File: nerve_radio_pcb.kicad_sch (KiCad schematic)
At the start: 12 parts, among them J1 2x15, J2 5V UART Breakout, J3 3V SPI Breakout, J4 5V GPIO Breakout, U1 XBP9B-DMWT-002, U2 TXB0104QPWRQ1

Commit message: Fix board-to-board connector pinout
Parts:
- removed J1: 2x15, Connector_PinHeader_1.27mm:PinHeader_2x15_P1.27mm_Vertical_SMD, symbol Connector_Generic:Conn_02x15_Counter_Clockwise
- added J1: 2x15, Connector_PinHeader_1.27mm:PinHeader_2x15_P1.27mm_Vertical_SMD, symbol Connector_Generic:Conn_02x15_Odd_Even
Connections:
- net +3V3: now also J1.3 (Pin_3), J1.4 (Pin_4)
- net +5V: now also J1.1 (Pin_1), J1.2 (Pin_2)
- net GND: now also J1.10 (Pin_10), J1.13 (Pin_13), J1.14 (Pin_14), J1.19 (Pin_19), J1.20 (Pin_20), J1.22 (Pin_22), J1.23 (Pin_23), J1.26 (Pin_26), J1.27 (Pin_27), J1.5 (Pin_5), J1.7 (Pin_7)
- net GPIO_1: now also J1.16 (Pin_16)
- net GPIO_2: now also J1.18 (Pin_18)
- net RADIO_NRST: now also J1.12 (Pin_12)
- net RADIO_UART_CTS: now also J1.11 (Pin_11)
- net RADIO_UART_RTS: now also J1.9 (Pin_9)
- net RADIO_UART_RX: now also J1.8 (Pin_8)
- net RADIO_UART_TX: now also J1.6 (Pin_6)
- net SPI_CLK: now also J1.17 (Pin_17)
- net SPI_CS: now also J1.15 (Pin_15)
- net SPI_MISO: now also J1.21 (Pin_21)
- net SPI_MOSI: now also J1.25 (Pin_25)
- net UART_RX: now also J1.24 (Pin_24)
- net UART_TX: now also J1.28 (Pin_28)
- new net: J1.29 (Pin_29), J1.30 (Pin_30)

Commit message: Cleanup revision and docs pictures
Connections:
- net RADIO_UART_CTS: now also J1.8 (Pin_8); no longer J1.11 (Pin_11)
- net RADIO_UART_RTS: now also J1.6 (Pin_6); no longer J1.9 (Pin_9)
- net RADIO_UART_RX: now also J1.9 (Pin_9); no longer J1.8 (Pin_8)
- net RADIO_UART_TX: now also J1.11 (Pin_11); no longer J1.6 (Pin_6)

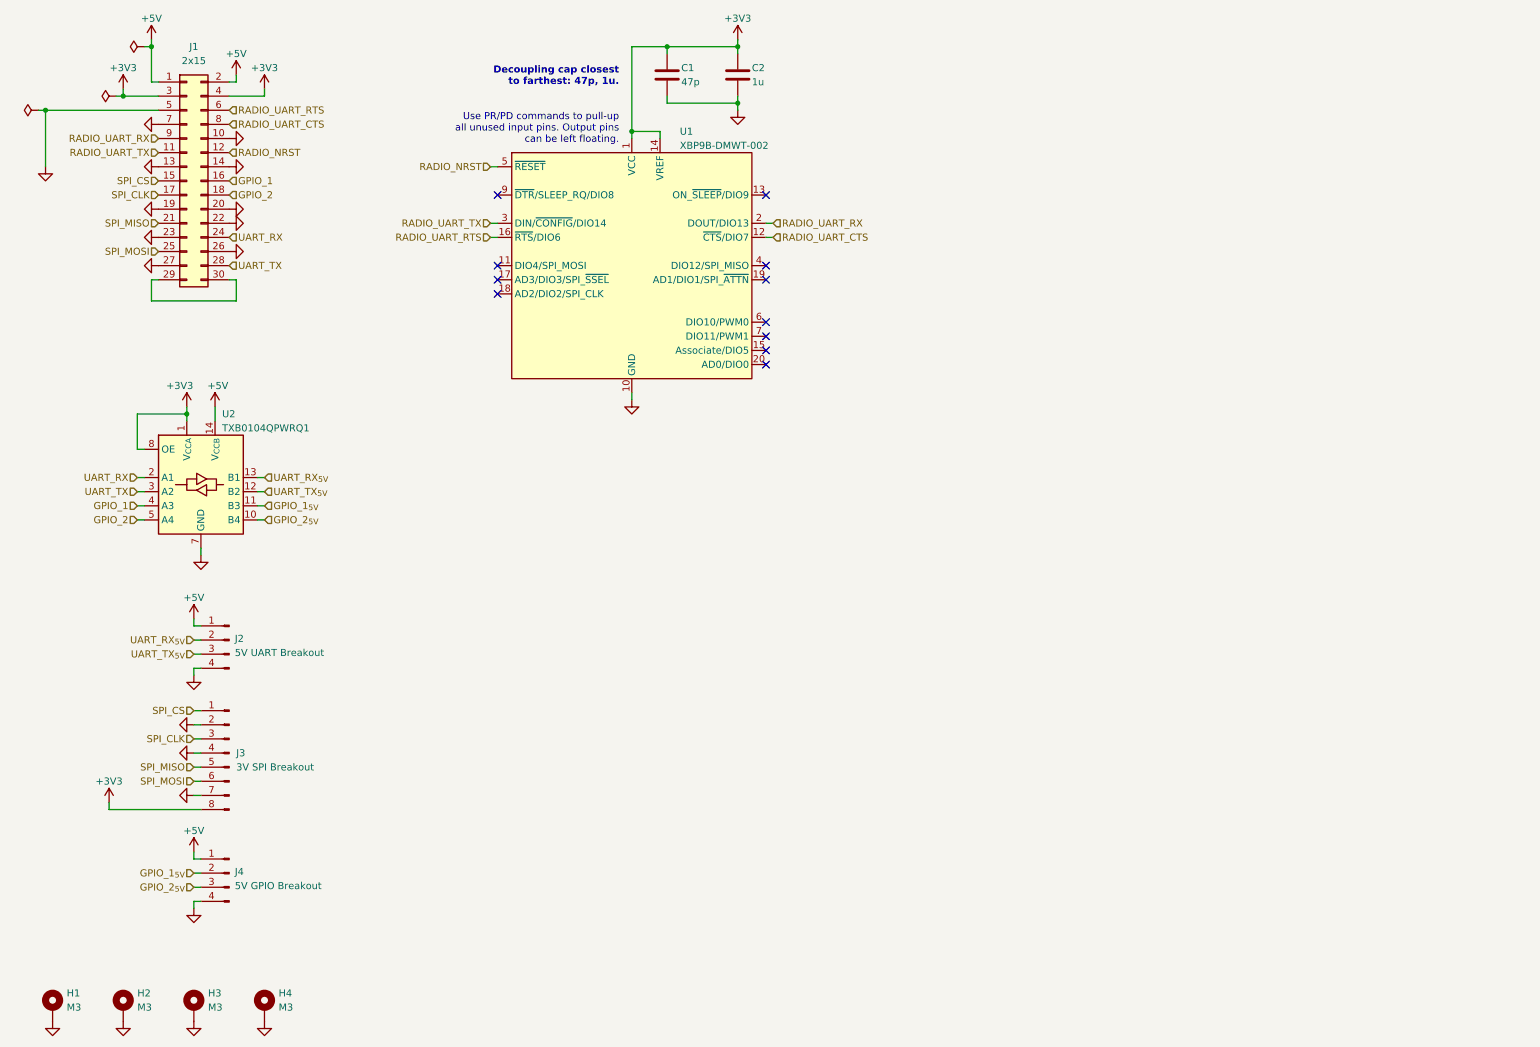
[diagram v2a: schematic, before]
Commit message: Cleanup and update board-to-board connector
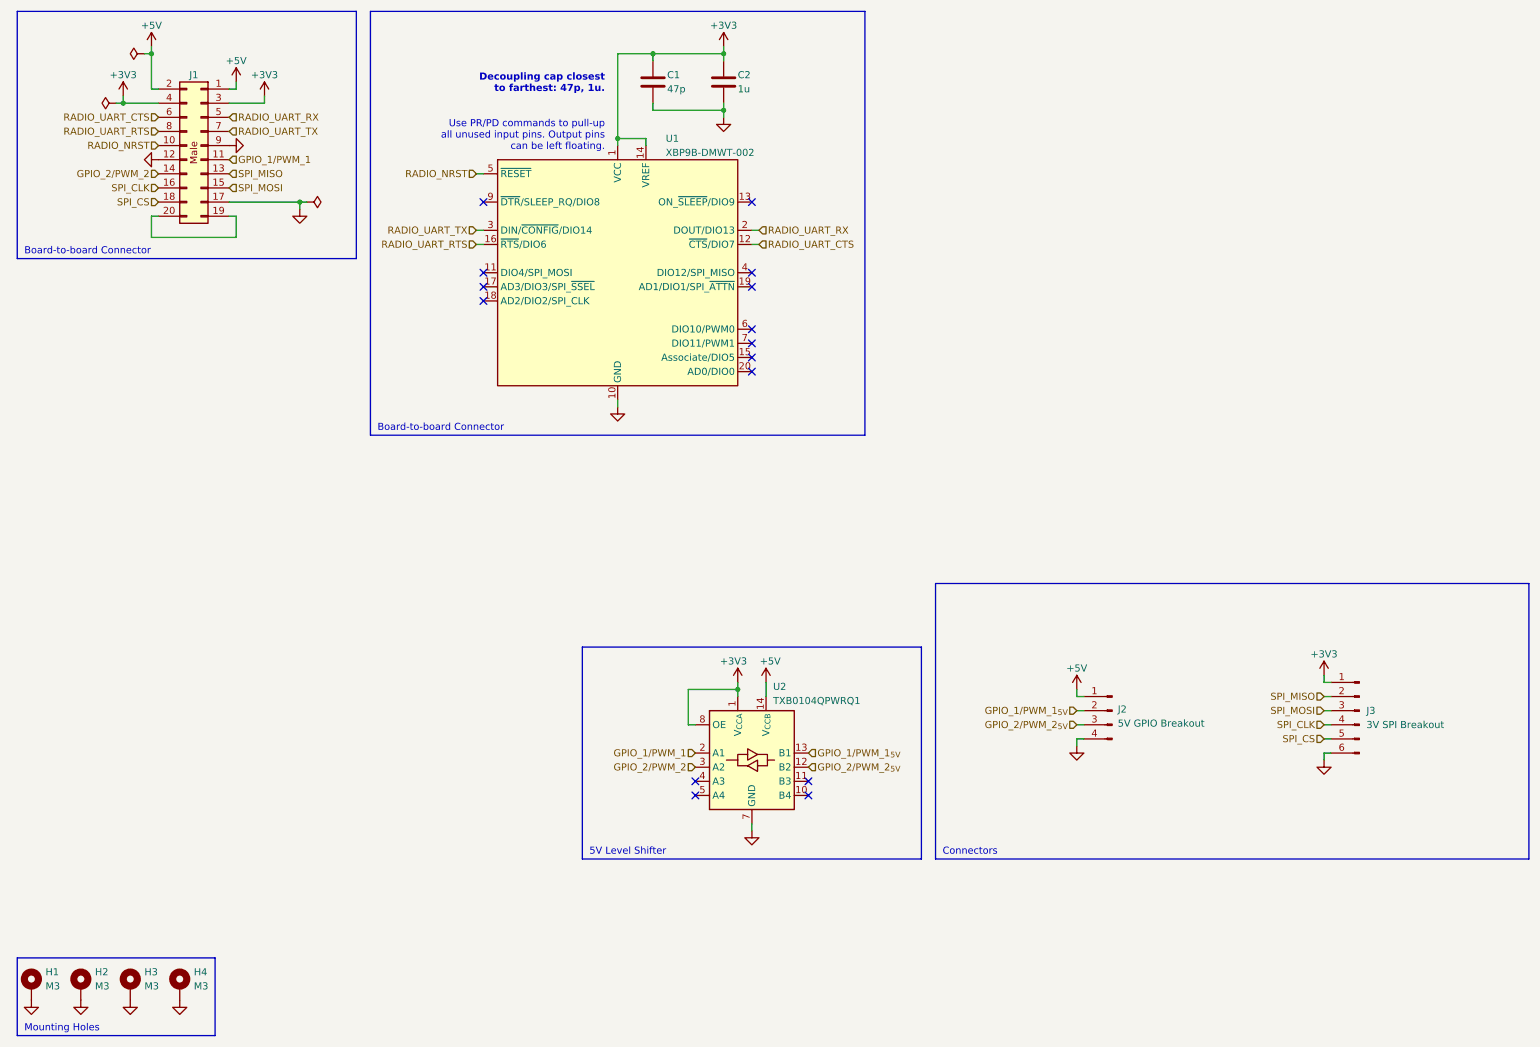
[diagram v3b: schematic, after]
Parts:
- removed J1: 2x15, Connector_PinHeader_1.27mm:PinHeader_2x15_P1.27mm_Vertical_SMD, symbol Connector_Generic:Conn_02x15_Odd_Even
- removed J2: 5V UART Breakout, Connector_PinHeader_2.54mm:PinHeader_1x04_P2.54mm_Vertical, symbol Connector:Conn_01x04_Pin
- removed J3: 3V SPI Breakout, Connector_PinHeader_2.54mm:PinHeader_1x08_P2.54mm_Vertical, symbol Connector:Conn_01x08_Pin
- added J1: BF030-20A-B1-0360-0277-0600-LB, connectors:bf030-20a-b1-0600-0277-0600-lb, symbol connectors:bf030-20a-b1-0360-0277-0600-lb
- added J3: 3V SPI Breakout, Connector_PinHeader_2.54mm:PinHeader_1x06_P2.54mm_Vertical, symbol Connector:Conn_01x06_Pin
- renumbered J4 to J2
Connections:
- net +3V3: now also J1.3, J1.4, J3.1 (Pin_1)
- net +5V: now also J1.1, J1.2
- net GND: now also J1.12, J1.17, J1.9, J3.6 (Pin_6)
- net RADIO_NRST: now also J1.10
- net RADIO_UART_CTS: now also J1.6
- net RADIO_UART_RTS: now also J1.8
- net RADIO_UART_RX: now also J1.5
- net RADIO_UART_TX: now also J1.7
- net SPI_CLK: now also J1.16, J3.4 (Pin_4)
- net SPI_CS: now also J1.18, J3.5 (Pin_5)
- net SPI_MISO: now also J1.13, J3.2 (Pin_2)
- net SPI_MOSI: now also J1.15, J3.3 (Pin_3)
- net GPIO_1: no longer names the net of U2.4 (A3)
- net GPIO_1_{5V}: no longer names the net of U2.11 (B3)
- net GPIO_1_{5V}: no longer J2.2 (Pin_2)
- net GPIO_2: no longer names the net of U2.5 (A4)
- net GPIO_2_{5V}: no longer names the net of U2.10 (B4)
- net GPIO_2_{5V}: no longer J2.3 (Pin_3)
- net UART_RX renamed GPIO_1/PWM_1
- net GPIO_1/PWM_1: now also J1.11
- net UART_RX_{5V} renamed GPIO_1/PWM_1_{5V}
- net GPIO_1/PWM_1_{5V}: now also J2.2 (Pin_2)
- net UART_TX renamed GPIO_2/PWM_2
- net GPIO_2/PWM_2: now also J1.14
- net UART_TX_{5V} renamed GPIO_2/PWM_2_{5V}
- net GPIO_2/PWM_2_{5V}: now also J2.3 (Pin_3)
- new net: J1.19, J1.20
- no-connect marks 11 -> 15
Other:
- note added: "5V Level Shifter"
- note added: "Board-to-board Connector"
- note added: "Connectors"
- note added: "Mounting Holes"
- moved on the sheet: C1, C2, J2, U1

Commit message: Update config.kibot.yaml, cleanup, add fiducials
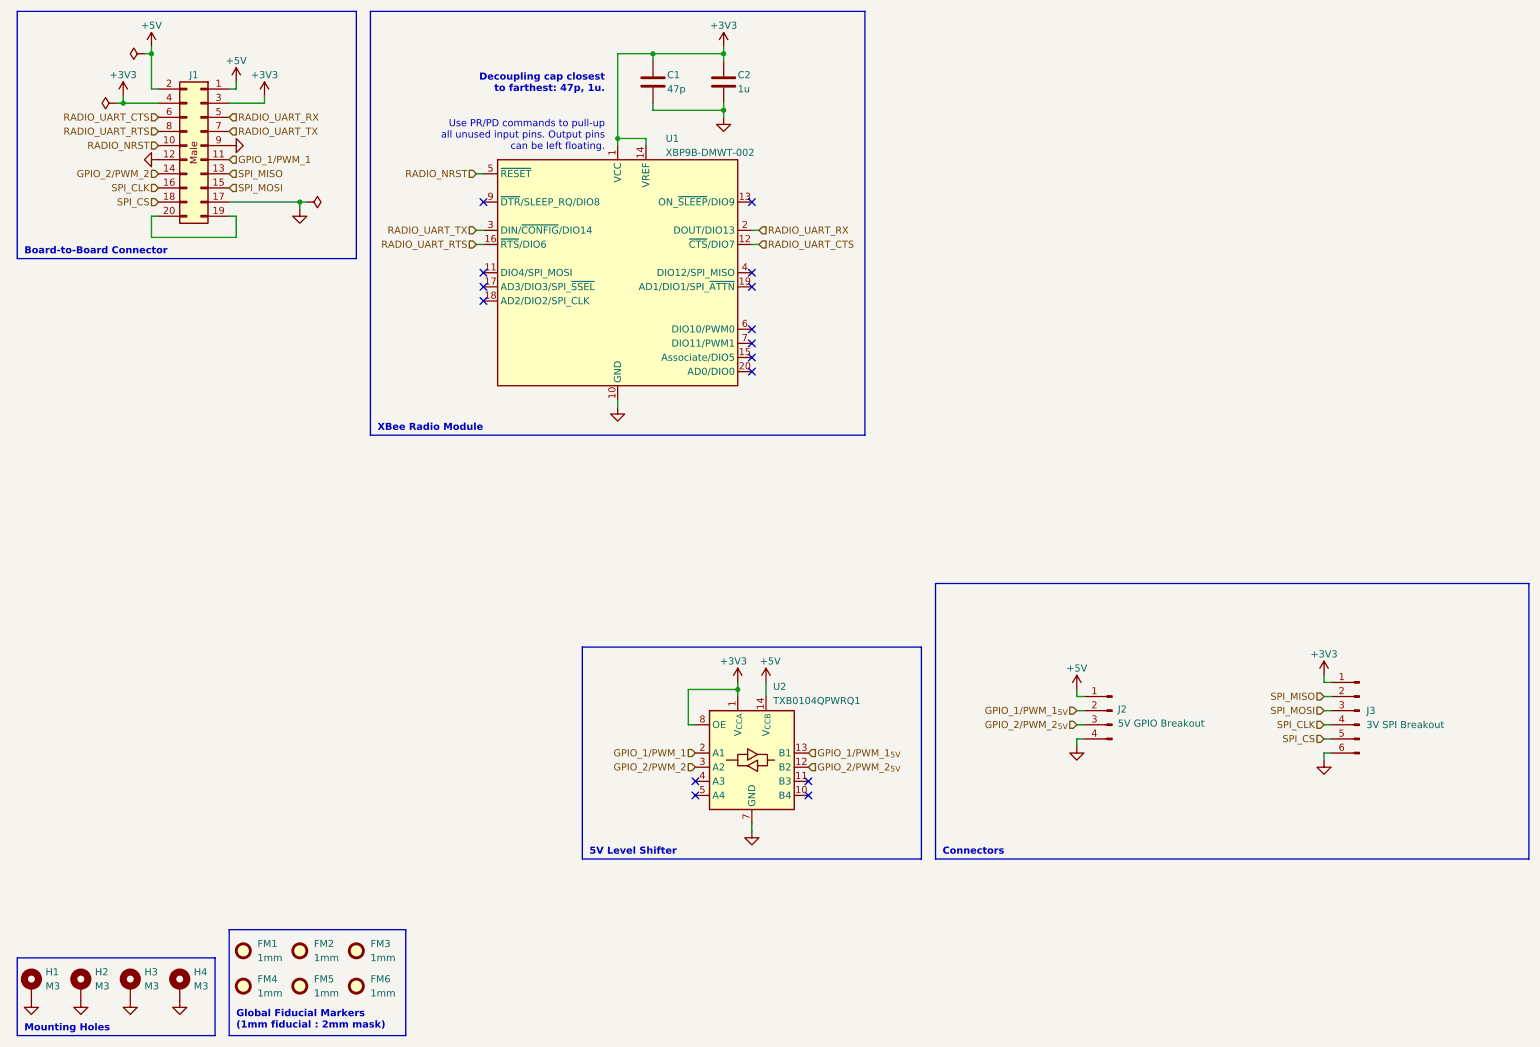
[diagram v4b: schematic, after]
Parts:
- added FM1, FM2, FM3, FM4, FM5, FM6: 1mm, Fiducial:Fiducial_1mm_Mask2mm, symbol Mechanical:Fiducial
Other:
- note added: "Board-to-Board Connector"
- note added: "Global Fiducial Markers (1mm fiducial : 2mm mask)"
- note added: "XBee Radio Module"
- note removed: "Board-to-board Connector"

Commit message: Update component_library and add 5V buck
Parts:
- added C1: 10u, Capacitor_SMD:C_0805_2012Metric, symbol Device:C
- added C2: 22u, Capacitor_SMD:C_0805_2012Metric, symbol Device:C
- added C3: 16n, Capacitor_SMD:C_0603_1608Metric, symbol Device:C
- added R1, R2: 76k8, Resistor_SMD:R_0603_1608Metric, symbol Device:R
- added TP1: TestPoint, TestPoint:TestPoint_Pad_D2.0mm, symbol Connector:TestPoint
- added U2: TPSM82903, ti_buck:tpsm8290x, symbol ti_buck:tpsm82903
- renumbered C1 to C4, C2 to C5, U2 to U1, U1 to U3
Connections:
- net +5V: now also C2.1, U2.10 (VOUT), U2.9 (VOUT)
- net GND: now also C1.2, C2.2, C3.2, R1.2, R2.2, U2.11 (GND)
- net GPIO_1/PWM_1: now also U1.4 (A3); no longer U1.2 (A1)
- net GPIO_1/PWM_1_{5V}: now also U1.11 (B3); no longer U1.13 (B1)
- net GPIO_2/PWM_2: now also U1.5 (A4); no longer U1.3 (A2)
- net GPIO_2/PWM_2_{5V}: now also U1.10 (B4); no longer U1.12 (B2)
- new net: R2.1, U2.4 (MODE/S-CONF)
- new net: C3.1, U2.5 (SS/TR)
- new net: TP1.1, U2.6 (PG)
- new net: R1.1, U2.7 (FB/VSET)
- new net +VSUPPLY: C1.1, U2.1 (VIN), U2.2 (VIN), U2.3 (EN)
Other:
- note added: "5V Buck Converter"
- note added: "MODE/S-CONFIG Resistor Setting: - FB/VSET-Pin: VSET mode - R_{MODE/S-CONF} = 76.8kΩ - F_{SW} = 1 MHz - Output discharge: Yes - Mode: Forced PWM - Dynamic mode change: Not active"
- note added: "Resistors: E96 Resistor Series, 1% Accuracy, Temperature Coefficient better or equal than ±200 ppm/°C C_{VIN} suggested: 0805 C_{VOUT} suggested: 0805"
- note added: "Soft start time C_{SS} = T_{SS} * I_{SS} / V_{REF} I_{SS} = 2.5uA V_{REF} = V_{FB}/0.75 V_{REF} = 0.6V / 0.75 = 0.8V For T_{SS} = 5ms: C_{SS} = 15.625nF"
- note added: "VSET Mode (5V) - R_{VSET} = 76.8kΩ"
- moved on the sheet: C4, C5, U1, U3

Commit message: Cleanup and add battery connector
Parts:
- added J4: Battery, radio_pcb_connectors:battery, symbol Connector:Conn_01x02_Pin
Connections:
- net +VSUPPLY: now also J4.2 (Pin_2)
- net GND: now also J4.1 (Pin_1)
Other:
- moved on the sheet: J2, J3
